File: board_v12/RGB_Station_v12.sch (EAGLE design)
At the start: 44 parts, among them IC1 MCP1702T-3302E/MB, J1 M20, J2 M20, J3 USB_MICRO, SW1 KMR2_SWITCH, SW2 KMR2_SWITCH, U1 PIC32MX270F256D_44VTLA_44, U2 74LVC2T45, U3 MCP121T-315E/TT, U4 DSC6111CI1A-008.0000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

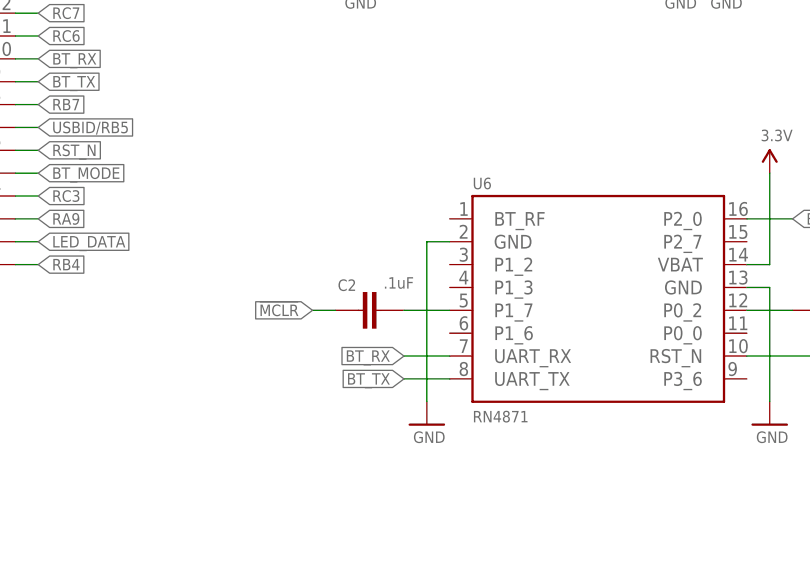
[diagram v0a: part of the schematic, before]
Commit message: Updates to v1.2 : Made two screw terminals DNPs, and changed C2 from .1uf to 1uF to help with preventing resetting of PIC32 when RN does firmware update.
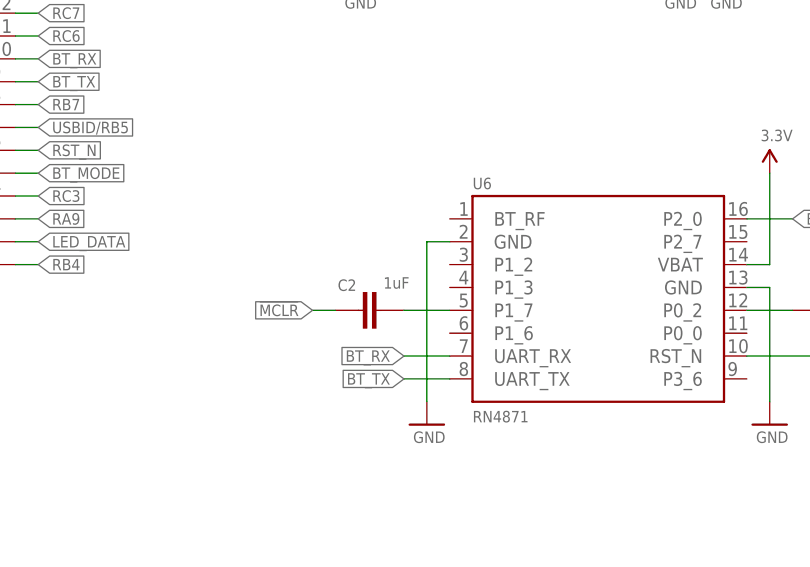
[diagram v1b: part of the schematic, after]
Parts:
- C2: value .1uF -> 1uF
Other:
- note added: "D.N.P"
- note added: "v1.2 Dec 14, 2017 Fixed schematic with shorted switches J5, J6 now DNP C2 now 1uF"
- note removed: "v1.2 Dec 14, 2017 Fixed schematic with shorted switches"
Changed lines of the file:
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@@
 <?xml version="1.0" encoding="utf-8"?>
 <!DOCTYPE eagle SYSTEM "eagle.dtd">
-<eagle version="7.7.0">
+<eagle version="8.6.2">
 <drawing>
 <settings>
 <setting alwaysvectorfont="no"/>
+<setting keepoldvectorfont="yes"/>
 <setting verticaltext="up"/>
 </settings>
@@
 <part name="P+13" library="SparkFun02-20-08" deviceset="3.3V" device=""/>
 <part name="GND34" library="SparkFun02-20-08" deviceset="GND" device=""/>
-<part name="C2" library="SparkFun-Capacitors" deviceset="CAP" device="0603-CAP" value=".1uF"/>
+<part name="C2" library="SparkFun-Capacitors" deviceset="CAP" device="0603-CAP" value="1uF"/>
 <part name="C6" library="SparkFun02-20-08" deviceset="CAP" device="0603" value="0.1uF"/>
 <part name="C12" library="SchmalzHaus" deviceset="CAP" device="0805" value="10uF"/>
@@
    Added pin numbers to output header silk
    Switched reset controller to SOT-23 (SC70 not available)</text>
-<text x="7.62" y="202.692" size="1.4224" layer="98">v1.2 Dec 14, 2017
-   Fixed schematic with shorted switches</text>
+<text x="66.04" y="220.472" size="1.4224" layer="98">v1.2 Dec 14, 2017
+   Fixed schematic with shorted switches
+   J5, J6 now DNP
+   C2 now 1uF</text>
+<text x="39.878" y="50.292" size="1.778" layer="98">D.N.P</text>
+<text x="359.664" y="161.29" size="1.27" layer="98" font="vector">D.N.P</text>
+<text x="360.934" y="183.896" size="1.27" layer="98" font="vector">D.N.P</text>
 </plain>
 <instances>

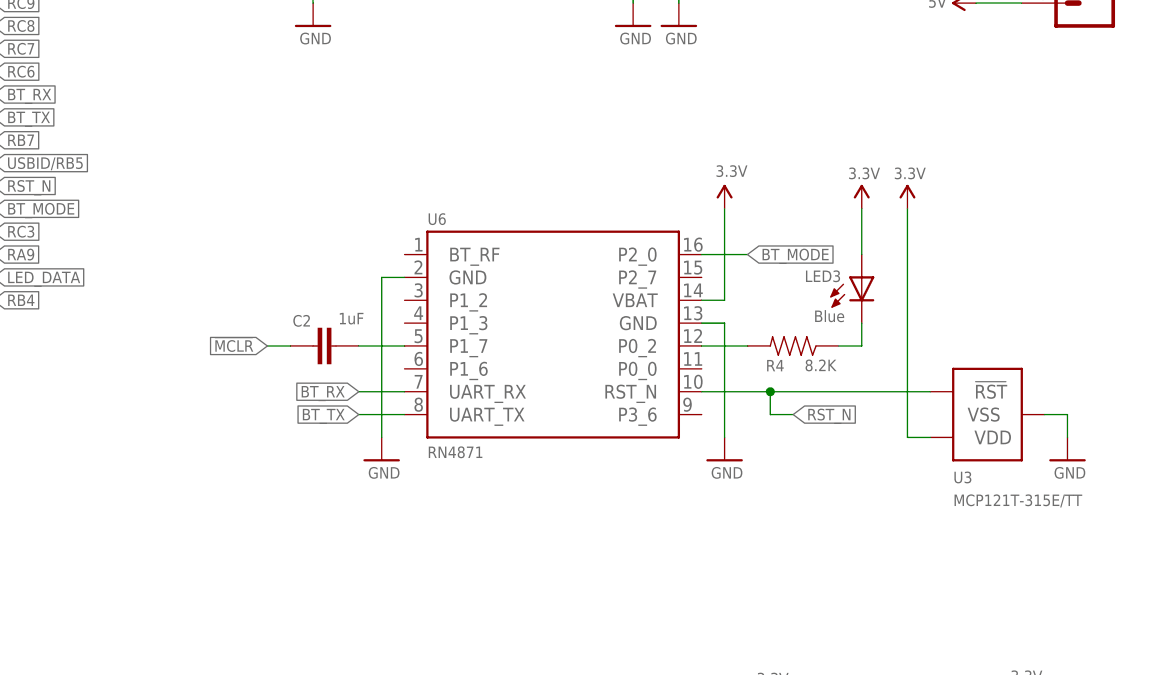
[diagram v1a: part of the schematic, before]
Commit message: Updated v1.2 board for PCB:NG production - changed DRC rules to minimize violations. Updated .1uF cap and red LED with alternate parts. Updated USB footprint to be exactly correct for Wurth USB connector from BOM
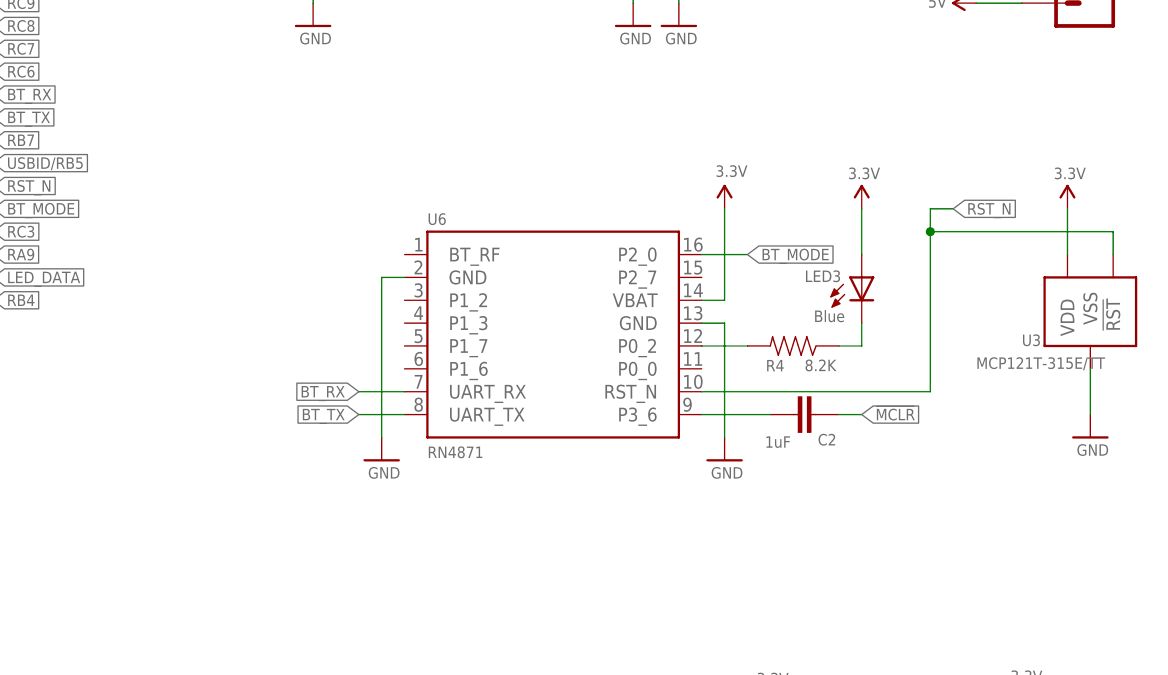
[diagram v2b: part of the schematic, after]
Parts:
- IC1: device linear:MCP170333MB -> RGB_Station_v12:LINEAR_MCP170328MB
- J3: device SparkFun-Connectors:USB_MICRO-B_FEMALE-SMT -> RGB_Station_v12:SPARKFUN-CONNECTORS_USB_MICRO-B_FEMALE-SMT
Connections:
- removed net N$8: C2.1, U6.P1_7
- new net N$7: C2.1, U6.P3_6
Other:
- moved on the sheet: C2, U3
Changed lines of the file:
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@@
 <?xml version="1.0" encoding="utf-8"?>
 <!DOCTYPE eagle SYSTEM "eagle.dtd">
-<eagle version="8.6.2">
+<eagle version="8.6.3">
 <drawing>
 <settings>
@@
 <layer number="59" name="tCarbon" color="7" fill="1" visible="no" active="no"/>
 <layer number="60" name="bCarbon" color="7" fill="1" visible="no" active="no"/>
+<layer number="88" name="SimResults" color="9" fill="1" visible="yes" active="yes"/>
+<layer number="89" name="SimProbes" color="9" fill="1" visible="yes" active="yes"/>
 <layer number="90" name="Modules" color="5" fill="1" visible="yes" active="yes"/>
 <layer number="91" name="Nets" color="2" fill="1" visible="yes" active="yes"/>
@@
 <layer number="132" name="bAdjust" color="7" fill="1" visible="yes" active="yes"/>
 <layer number="144" name="Drill_legend" color="7" fill="1" visible="yes" active="yes"/>
+<layer number="145" name="DrillLegend_01-16" color="7" fill="1" visible="yes" active="yes"/>
+<layer number="146" name="DrillLegend_01-20" color="7" fill="1" visible="yes" active="yes"/>
 <layer number="150" name="Notes" color="7" fill="1" visible="yes" active="yes"/>
 <layer number="151" name="HeatSink" color="7" fill="1" visible="no" active="no"/>
@@
 <part name="J2" library="SchmalzHaus" deviceset="M20" device=""/>
 <part name="ICSP" library="SchmalzHaus" deviceset="M05" device="NOSLILK" value="J3"/>
-<part name="IC1" library="linear" deviceset="MCP1703*" device="MB" technology="33" value="MCP1702T-3302E/MB"/>
+<part name="IC1" library="RGB_Station_v12" deviceset="LINEAR_MCP1703*" device="MB" technology="28" value="MCP1702T-3302E/MB"/>
 <part name="GND1" library="SparkFun02-20-08" deviceset="GND" device=""/>
 <part name="U1" library="SchmalzHaus" deviceset="PIC32MX2XX_44" device="QFN44" value="PIC32MX270F256D_44VTLA_44"/>
@@
 <part name="GND29" library="SparkFun-Aesthetics" deviceset="GND" device=""/>
 <part name="U6" library="RN4870-71" deviceset="RN4871" device=""/>
-<part name="J3" library="SparkFun-Connectors" deviceset="USB_MICRO-B" device="_FEMALE-SMT" value="USB_MICRO"/>
+<part name="J3" library="RGB_Station_v12" deviceset="SPARKFUN-CONNECTORS_USB_MICRO-B" device="_FEMALE-SMT" value="USB_MICRO"/>
 <part name="J6" library="SparkFun-Connectors" deviceset="CONN_02" device="3.5MM"/>
 <part name="U3" library="MCP1x2_ResetController" deviceset="MCP1X2_RESET_CONTROLLER" device="" value="MCP121T-315E/TT"/>
@@
 <text x="11.43" y="198.628" size="1.27" layer="98" font="vector">Fubarino Mini (CPU and breadboard pins)</text>
 <text x="262.89" y="152.908" size="1.27" layer="98" font="vector">BLE module</text>
-<text x="347.98" y="109.728" size="1.27" layer="98" font="vector">Reset Controller</text>
+<text x="350.52" y="124.968" size="1.27" layer="98" font="vector">Reset Controller</text>
 <wire x1="78.74" y1="96.52" x2="154.94" y2="96.52" width="0.1524" layer="98"/>
 <wire x1="154.94" y1="96.52" x2="154.94" y2="63.5" width="0.1524" layer="98"/>
@@
 <attribute name="NAME" x="40.64" y="64.008" size="1.27" layer="95" font="vector"/>
 </instance>
-<instance part="U3" gate="G$1" x="353.06" y="121.92" smashed="yes">
-<attribute name="NAME" x="347.98" y="114.3" size="1.27" layer="95" font="vector"/>
-<attribute name="VALUE" x="347.98" y="111.76" size="1.27" layer="96" font="vector"/>
+<instance part="U3" gate="G$1" x="363.22" y="132.08" smashed="yes" rot="R270">
+<attribute name="NAME" x="355.6" y="129.54" size="1.27" layer="95" font="vector"/>
+<attribute name="VALUE" x="350.52" y="127" size="1.27" layer="96" font="vector"/>
 </instance>
 <instance part="GND10" gate="1" x="284.48" y="116.84" smashed="yes">
@@
 <attribute name="VALUE" x="321.056" y="114.808" size="1.27" layer="96" font="vector"/>
 </instance>
-<instance part="GND12" gate="1" x="360.68" y="116.84" smashed="yes">
-<attribute name="VALUE" x="359.156" y="114.808" size="1.27" layer="96" font="vector"/>
-</instance>
-<instance part="P+8" gate="G$1" x="342.9" y="144.78" smashed="yes">
-<attribute name="VALUE" x="341.376" y="148.082" size="1.27" layer="96" font="vector"/>
+<instance part="GND12" gate="1" x="363.22" y="119.38" smashed="yes">
+<attribute name="VALUE" x="361.696" y="117.348" size="1.27" layer="96" font="vector"/>
+</instance>
+<instance part="P+8" gate="G$1" x="360.68" y="144.78" smashed="yes">
+<attribute name="VALUE" x="359.156" y="148.082" size="1.27" layer="96" font="vector"/>
 </instance>
 <instance part="GND15" gate="1" x="53.34" y="27.94" smashed="yes">
@@
 <attribute name="VALUE" x="227.076" y="88.392" size="1.27" layer="96" font="vector"/>
 </instance>
-<instance part="C2" gate="G$1" x="276.86" y="129.54" smashed="yes" rot="R270">
-<attribute name="NAME" x="274.574" y="131.699" size="1.27" layer="95" font="vector"/>
-<attribute name="VALUE" x="279.654" y="131.953" size="1.27" layer="96" font="vector"/>
+<instance part="C2" gate="G$1" x="332.74" y="121.92" smashed="yes" rot="R90">
+<attribute name="NAME" x="335.026" y="119.761" size="1.27" layer="95" font="vector" rot="R180"/>
+<attribute name="VALUE" x="329.946" y="119.507" size="1.27" layer="96" font="vector" rot="R180"/>
 </instance>
 <instance part="C6" gate="G$1" x="106.68" y="78.74" smashed="yes">
@@
 <pinref part="U3" gate="G$1" pin="VSS"/>
 <pinref part="GND12" gate="1" pin="GND"/>
-<wire x1="358.14" y1="121.92" x2="360.68" y2="121.92" width="0.1524" layer="91"/>
-<wire x1="360.68" y1="121.92" x2="360.68" y2="119.38" width="0.1524" layer="91"/>
+<wire x1="363.22" y1="127" x2="363.22" y2="121.92" width="0.1524" layer="91"/>
 </segment>
 <segment>
@@
 <pinref part="U3" gate="G$1" pin="VDD"/>
 <pinref part="P+8" gate="G$1" pin="3.3V"/>
-<wire x1="345.44" y1="119.38" x2="342.9" y2="119.38" width="0.1524" layer="91"/>
-<wire x1="342.9" y1="119.38" x2="342.9" y2="144.78" width="0.1524" layer="91"/>
+<wire x1="360.68" y1="139.7" x2="360.68" y2="144.78" width="0.1524" layer="91"/>
 </segment>
 <segment>
@@
 <segment>
 <pinref part="C2" gate="G$1" pin="2"/>
-<wire x1="274.32" y1="129.54" x2="271.78" y2="129.54" width="0.1524" layer="91"/>
-<label x="271.78" y="129.54" size="1.27" layer="95" font="vector" rot="R180" xref="yes"/>
+<wire x1="335.28" y1="121.92" x2="337.82" y2="121.92" width="0.1524" layer="91"/>
+<label x="337.82" y="121.92" size="1.27" layer="95" font="vector" xref="yes"/>
 </segment>
 </net>
@@
 <pinref part="U3" gate="G$1" pin="!RST!"/>
 <pinref part="U6" gate="G$1" pin="RST_N"/>
-<label x="330.2" y="121.92" size="1.27" layer="95" font="vector" xref="yes"/>
-<wire x1="345.44" y1="124.46" x2="327.66" y2="124.46" width="0.1524" layer="91"/>
-<wire x1="327.66" y1="124.46" x2="320.04" y2="124.46" width="0.1524" layer="91"/>
-<wire x1="327.66" y1="124.46" x2="327.66" y2="121.92" width="0.1524" layer="91"/>
-<junction x="327.66" y="124.46"/>
-<wire x1="327.66" y1="121.92" x2="330.2" y2="121.92" width="0.1524" layer="91"/>
+<label x="347.98" y="144.78" size="1.27" layer="95" font="vector" xref="yes"/>
+<wire x1="365.76" y1="139.7" x2="365.76" y2="142.24" width="0.1524" layer="91"/>
+<wire x1="365.76" y1="142.24" x2="345.44" y2="142.24" width="0.1524" layer="91"/>
+<wire x1="345.44" y1="142.24" x2="345.44" y2="124.46" width="0.1524" layer="91"/>
+<wire x1="345.44" y1="124.46" x2="320.04" y2="124.46" width="0.1524" layer="91"/>
+<wire x1="345.44" y1="142.24" x2="345.44" y2="144.78" width="0.1524" layer="91"/>
+<junction x="345.44" y="142.24"/>
+<wire x1="345.44" y1="144.78" x2="347.98" y2="144.78" width="0.1524" layer="91"/>
 </segment>
 <segment>
@@
 <pinref part="J2" gate="G$1" pin="5"/>
 <label x="241.3" y="144.78" size="1.27" layer="95" font="vector" xref="yes"/>
-</segment>
-</net>
-<net name="N$8" class="0">
-<segment>
-<pinref part="U6" gate="G$1" pin="P1_7"/>
-<pinref part="C2" gate="G$1" pin="1"/>
-<wire x1="287.02" y1="129.54" x2="281.94" y2="129.54" width="0.1524" layer="91"/>
 </segment>
 </net>
@@
 </segment>
 </net>
+<net name="N$7" class="0">
+<segment>
+<pinref part="C2" gate="G$1" pin="1"/>
+<pinref part="U6" gate="G$1" pin="P3_6"/>
+<wire x1="327.66" y1="121.92" x2="320.04" y2="121.92" width="0.1524" layer="91"/>
+</segment>
+</net>

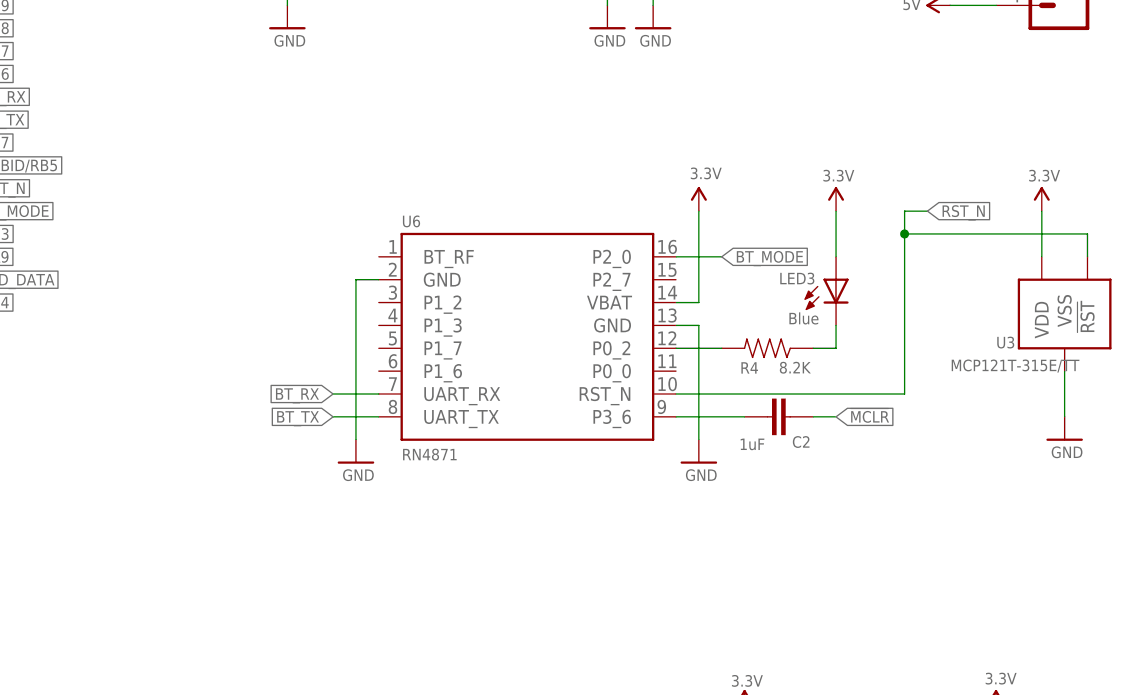
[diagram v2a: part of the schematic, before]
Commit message: Updated note on schematic about using open-drain reset controller, not push-pull.
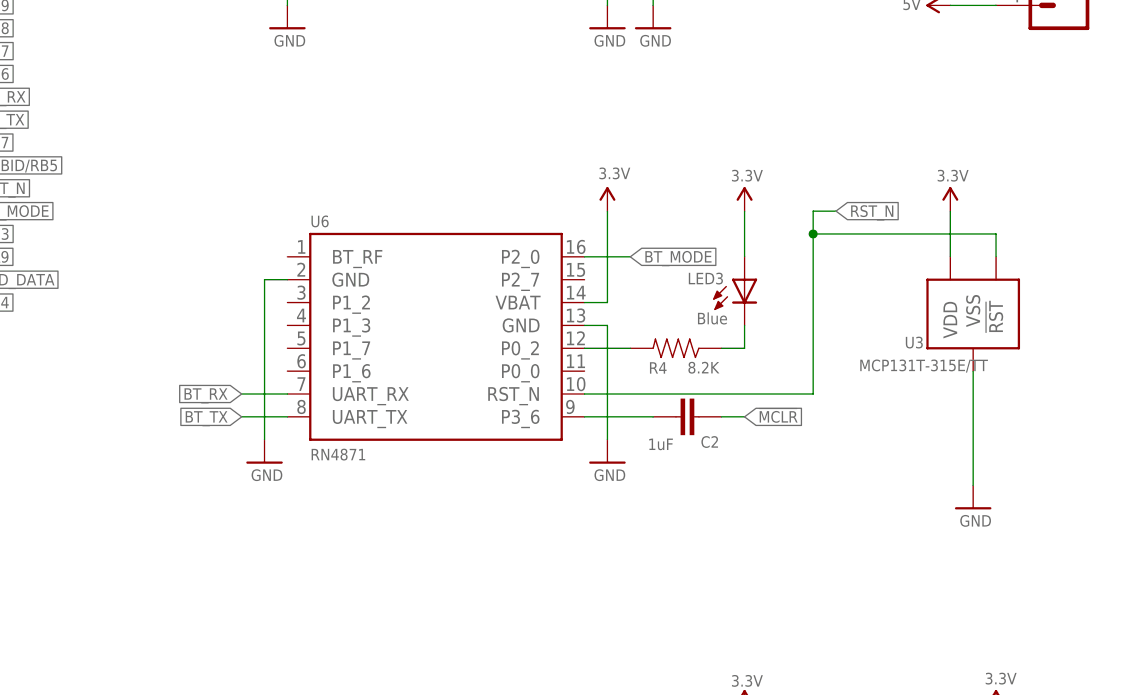
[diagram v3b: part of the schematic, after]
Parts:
- U3: value MCP121T-315E/TT -> MCP131T-315E/TT
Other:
- note added: "Reset Controller (critical to use MCP121 or MCP131 varient, as they are open drain, not push-pull outputs.)"
- note added: "v1.2 Feb 19, 2018 Fixed schematic with shorted switches J5, J6 now DNP C2 now 1uF P3_6 now used to reset PIC32"
- note removed: "Reset Controller"
- note removed: "v1.2 Dec 14, 2017 Fixed schematic with shorted switches J5, J6 now DNP C2 now 1uF"
- moved on the sheet: C2, LED3, R4, U3, U6

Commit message: Finished centroid file for PCB:NG automation. Updated some library footprints.
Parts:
- IC1: device RGB_Station_v12:LINEAR_MCP170328MB -> RGB_Station_v12_VREG:RGB_STATION_V12_LINEAR_MCP170328MB
- J3: device RGB_Station_v12:SPARKFUN-CONNECTORS_USB_MICRO-B_FEMALE-SMT -> RGB_Station_v12_USB_CONN:SPARKFUN-CONNECTORS_USB_MICRO-B_FEMALE-SMT
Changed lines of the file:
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@@
 <?xml version="1.0" encoding="utf-8"?>
 <!DOCTYPE eagle SYSTEM "eagle.dtd">
-<eagle version="8.6.3">
+<eagle version="8.7.0">
 <drawing>
 <settings>
@@
 <part name="J2" library="SchmalzHaus" deviceset="M20" device=""/>
 <part name="ICSP" library="SchmalzHaus" deviceset="M05" device="NOSLILK" value="J3"/>
-<part name="IC1" library="RGB_Station_v12" deviceset="LINEAR_MCP1703*" device="MB" technology="28" value="MCP1702T-3302E/MB"/>
+<part name="IC1" library="RGB_Station_v12_VREG" deviceset="RGB_STATION_V12_LINEAR_MCP1703*" device="MB" technology="28" value="MCP1702T-3302E/MB"/>
 <part name="GND1" library="SparkFun02-20-08" deviceset="GND" device=""/>
 <part name="U1" library="SchmalzHaus" deviceset="PIC32MX2XX_44" device="QFN44" value="PIC32MX270F256D_44VTLA_44"/>
@@
 <part name="GND29" library="SparkFun-Aesthetics" deviceset="GND" device=""/>
 <part name="U6" library="RN4870-71" deviceset="RN4871" device=""/>
-<part name="J3" library="RGB_Station_v12" deviceset="SPARKFUN-CONNECTORS_USB_MICRO-B" device="_FEMALE-SMT" value="USB_MICRO"/>
+<part name="J3" library="RGB_Station_v12_USB_CONN" deviceset="SPARKFUN-CONNECTORS_USB_MICRO-B" device="_FEMALE-SMT" value="USB_MICRO"/>
 <part name="J6" library="SparkFun-Connectors" deviceset="CONN_02" device="3.5MM"/>
 <part name="U3" library="MCP1x2_ResetController" deviceset="MCP1X2_RESET_CONTROLLER" device="" value="MCP131T-315E/TT"/>
